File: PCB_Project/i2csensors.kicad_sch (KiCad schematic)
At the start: 19 parts, among them J2 ZE27-O3, J3 Motor_Connector, J4 Motor_Connector, J5 Motor_Connector, J6 Motor_Connector

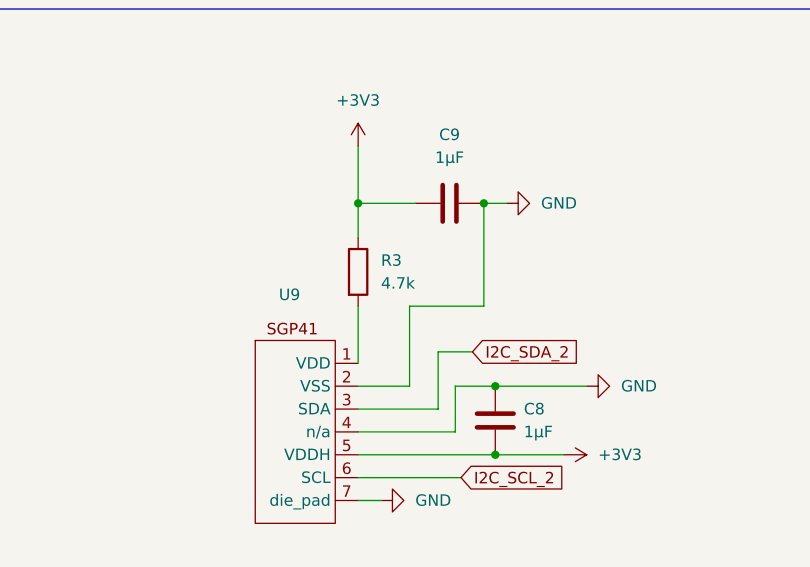
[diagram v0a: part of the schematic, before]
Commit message: Fixed resistor value for SGP41
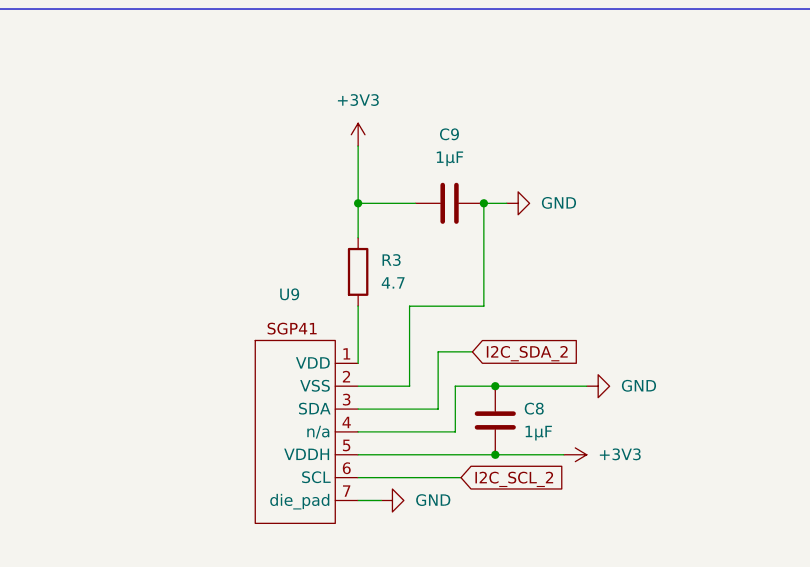
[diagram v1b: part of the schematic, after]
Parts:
- R3: value 4.7k -> 4.7
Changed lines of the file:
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@@
 			)
 		)
-		(property "Value" "4.7k"
+		(property "Value" "4.7"
 			(at 204.47 63.5 0)
 			(effects

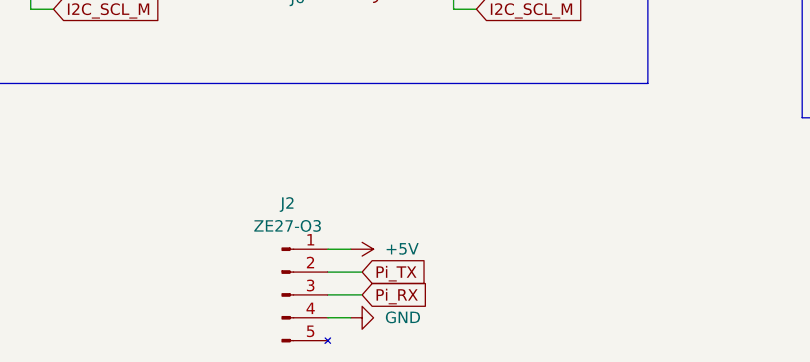
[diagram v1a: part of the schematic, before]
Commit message: Swapped Pi_RX and Pi_TX
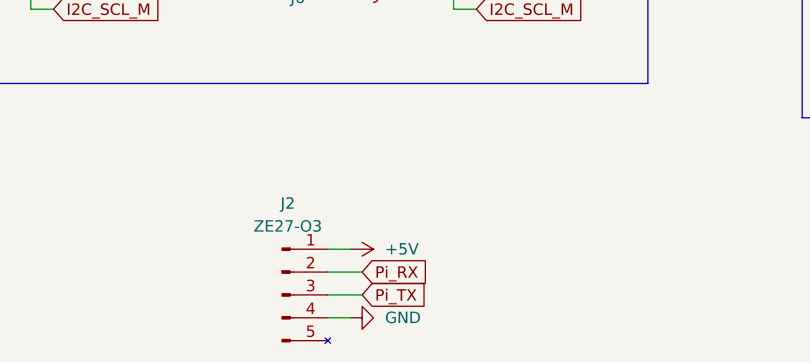
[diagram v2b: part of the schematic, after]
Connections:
- net Pi_RX: now also J2.2 (UART_TXD_(Out)); no longer J2.3 (UART_RX_(In))
- net Pi_TX: now also J2.3 (UART_RX_(In)); no longer J2.2 (UART_TXD_(Out))
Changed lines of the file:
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@@
 	(global_label "Pi_TX"
 		(shape input)
-		(at 93.98 162.56 0)
+		(at 93.98 165.1 0)
 		(fields_autoplaced yes)
 		(effects
@@
 		)
 		(property "Intersheetrefs" "${INTERSHEET_REFS}"
-			(at 101.9847 162.56 0)
+			(at 101.9847 165.1 0)
 			(effects
 				(font
@@
 	(global_label "Pi_RX"
 		(shape input)
-		(at 93.98 165.1 0)
+		(at 93.98 162.56 0)
 		(fields_autoplaced yes)
 		(effects
@@
 		)
 		(property "Intersheetrefs" "${INTERSHEET_REFS}"
-			(at 102.2871 165.1 0)
+			(at 102.2871 162.56 0)
 			(effects
 				(font

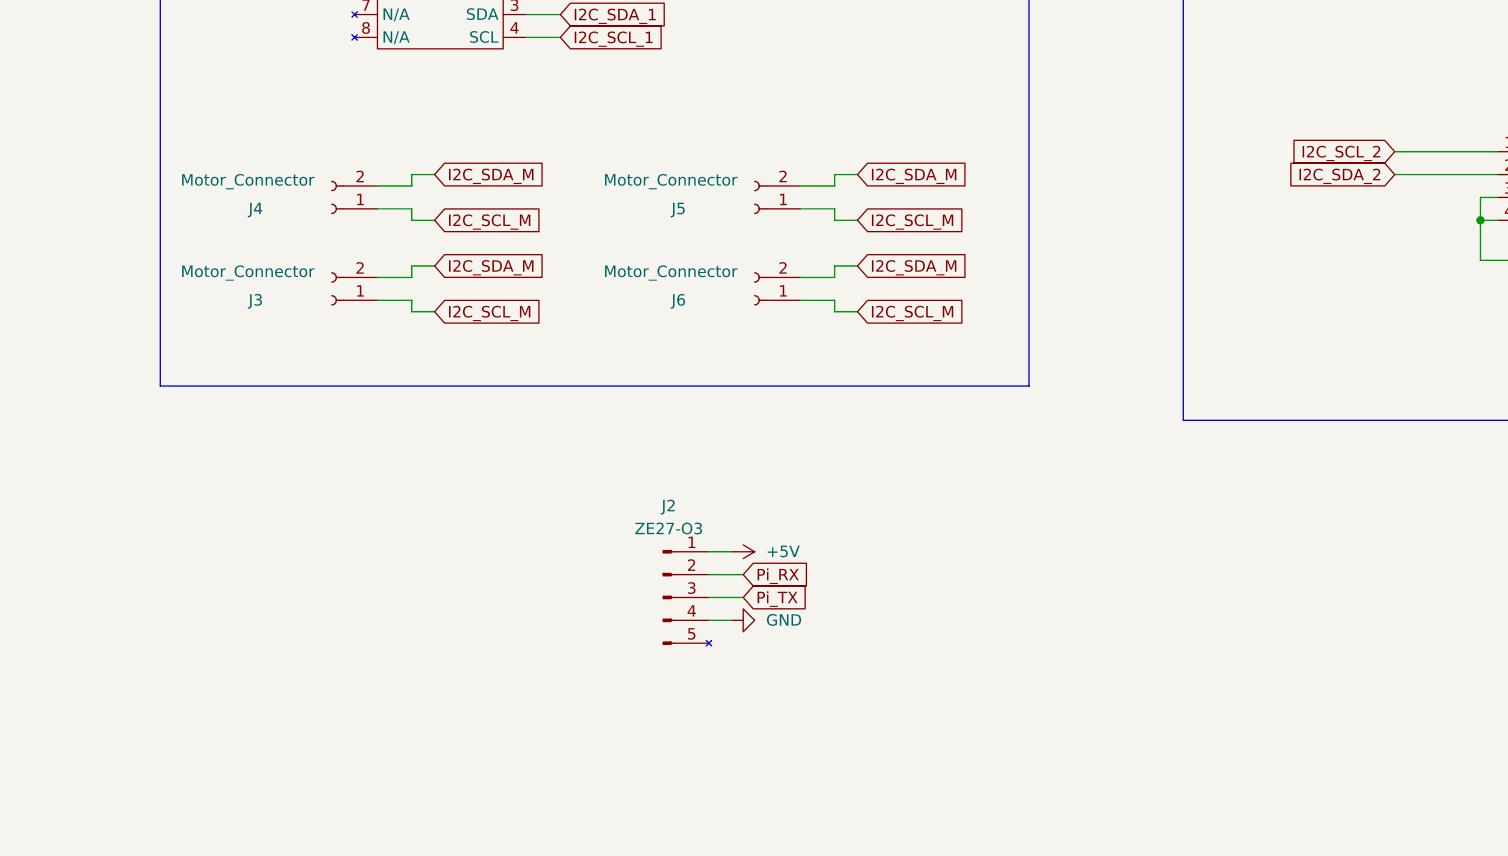
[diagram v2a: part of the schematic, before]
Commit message: added level shifters
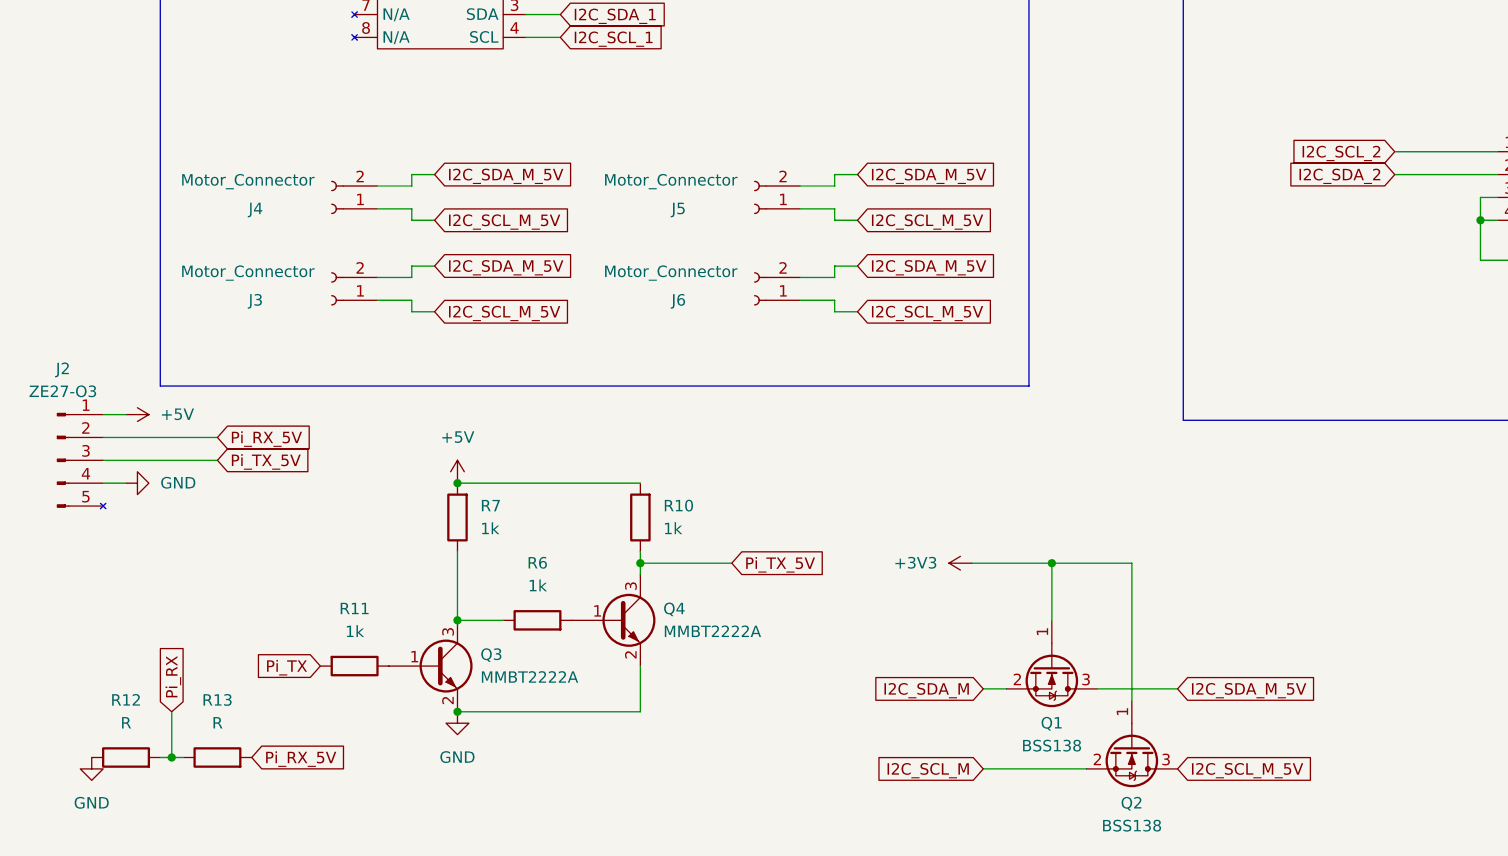
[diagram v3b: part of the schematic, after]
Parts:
- added Q1, Q2: BSS138, Package_TO_SOT_SMD:SOT-23, symbol Transistor_FET:BSS138
- added Q3, Q4: MMBT2222A, Package_TO_SOT_SMD:SOT-23, symbol Transistor_BJT:MMBT2222A
- added R10, R11, R6, R7: 1k, symbol Device:R
- added R12, R13: R, symbol Device:R
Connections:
- net +3V3: now also Q1.1 (G), Q2.1 (G)
- net +5V: now also R10.2, R7.2
- net GND: now also Q3.2 (E), Q4.2 (E), R12.1
- net I2C_SCL_M: now also Q2.2 (S); no longer J3.1 (Pin_1), J4.1 (Pin_1), J5.1 (Pin_1), J6.1 (Pin_1)
- net I2C_SDA_M: now also Q1.2 (S); no longer J3.2 (Pin_2), J4.2 (Pin_2), J5.2 (Pin_2), J6.2 (Pin_2)
- net Pi_RX: now also R12.2, R13.1; no longer J2.2 (UART_TXD_(Out))
- net Pi_TX: now also R11.2; no longer J2.3 (UART_RX_(In))
- new net: Q3.1 (B), R11.1
- new net: Q3.3 (C), R6.1, R7.1
- new net: Q4.1 (B), R6.2
- new net I2C_SCL_M_5V: J3.1 (Pin_1), J4.1 (Pin_1), J5.1 (Pin_1), J6.1 (Pin_1), Q2.3 (D)
- new net I2C_SDA_M_5V: J3.2 (Pin_2), J4.2 (Pin_2), J5.2 (Pin_2), J6.2 (Pin_2), Q1.3 (D)
- new net Pi_RX_5V: J2.2 (UART_TXD_(Out)), R13.2
- new net Pi_TX_5V: J2.3 (UART_RX_(In)), Q4.3 (C), R10.1
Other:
- moved on the sheet: J2

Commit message: footprints
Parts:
- R10, R11, R6, R7: footprint (none) -> Resistor_SMD:R_0402_1005Metric
- R12: value R -> 2k; footprint (none) -> Resistor_SMD:R_0402_1005Metric
- R13: value R -> 1k; footprint (none) -> Resistor_SMD:R_0402_1005Metric
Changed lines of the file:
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@@
 			)
 		)
-		(property "Value" "R"
+		(property "Value" "2k"
 			(at 25.4 179.07 90)
 			(effects
@@
 			)
 		)
-		(property "Footprint" ""
+		(property "Footprint" "Resistor_SMD:R_0402_1005Metric"
 			(at 25.4 184.658 90)
 			(effects
@@
 			)
 		)
-		(property "Footprint" ""
+		(property "Footprint" "Resistor_SMD:R_0402_1005Metric"
 			(at 50.8 170.942 90)
 			(effects
@@
 			)
 		)
-		(property "Footprint" ""
+		(property "Footprint" "Resistor_SMD:R_0402_1005Metric"
 			(at 84.328 156.21 90)
 			(effects
@@
 			)
 		)
-		(property "Footprint" ""
+		(property "Footprint" "Resistor_SMD:R_0402_1005Metric"
 			(at 64.008 156.21 90)
 			(effects
@@
 			)
 		)
-		(property "Footprint" ""
+		(property "Footprint" "Resistor_SMD:R_0402_1005Metric"
 			(at 71.12 169.418 90)
 			(effects
@@
 			)
 		)
-		(property "Value" "R"
+		(property "Value" "1k"
 			(at 35.56 179.07 90)
 			(effects
@@
 			)
 		)
-		(property "Footprint" ""
+		(property "Footprint" "Resistor_SMD:R_0402_1005Metric"
 			(at 35.56 184.658 90)
 			(effects

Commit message: soldering it to the board
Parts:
- J2: footprint Connector_JST:JST_EH_B5B-EH-A_1x05_P2.50mm_Vertical -> Connector_PinHeader_2.00mm:PinHeader_1x05_P2.00mm_Vertical
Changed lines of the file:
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@@
 			)
 		)
-		(property "Footprint" "Connector_JST:JST_EH_B5B-EH-A_1x05_P2.50mm_Vertical"
+		(property "Footprint" "Connector_PinHeader_2.00mm:PinHeader_1x05_P2.00mm_Vertical"
 			(at 17.78 149.86 0)
 			(effects

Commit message: working on final board
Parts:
- removed J2: ZE27-O3, Connector_PinHeader_2.00mm:PinHeader_1x05_P2.00mm_Vertical, symbol Connector:Conn_01x05_Pin
- removed Q1, Q2: BSS138, Package_TO_SOT_SMD:SOT-23, symbol Transistor_FET:BSS138
- removed Q3, Q4: MMBT2222A, Package_TO_SOT_SMD:SOT-23, symbol Transistor_BJT:MMBT2222A
- removed R10, R11, R13, R6, R7: 1k, Resistor_SMD:R_0402_1005Metric, symbol Device:R
- removed R12: 2k, Resistor_SMD:R_0402_1005Metric, symbol Device:R
- C2: renamed from C11; value 1 µF -> 1µF
- U6: renamed from U11; footprint Sensor:SOIC127P600X175-8N_ADT7410TRZ-REEL -> Sensor:SOIC127P600X175-8N
- renumbered C12 to C1, C9 to C3, C10 to C4, C8 to C5, C15 to C6, C13 to C7, C14 to C8, J4 to J1, J5 to J2, J6 to J4, R3 to R7, U12 to U2, U9 to U3, U8 to U4, U10 to U5
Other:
- moved on the sheet: C3

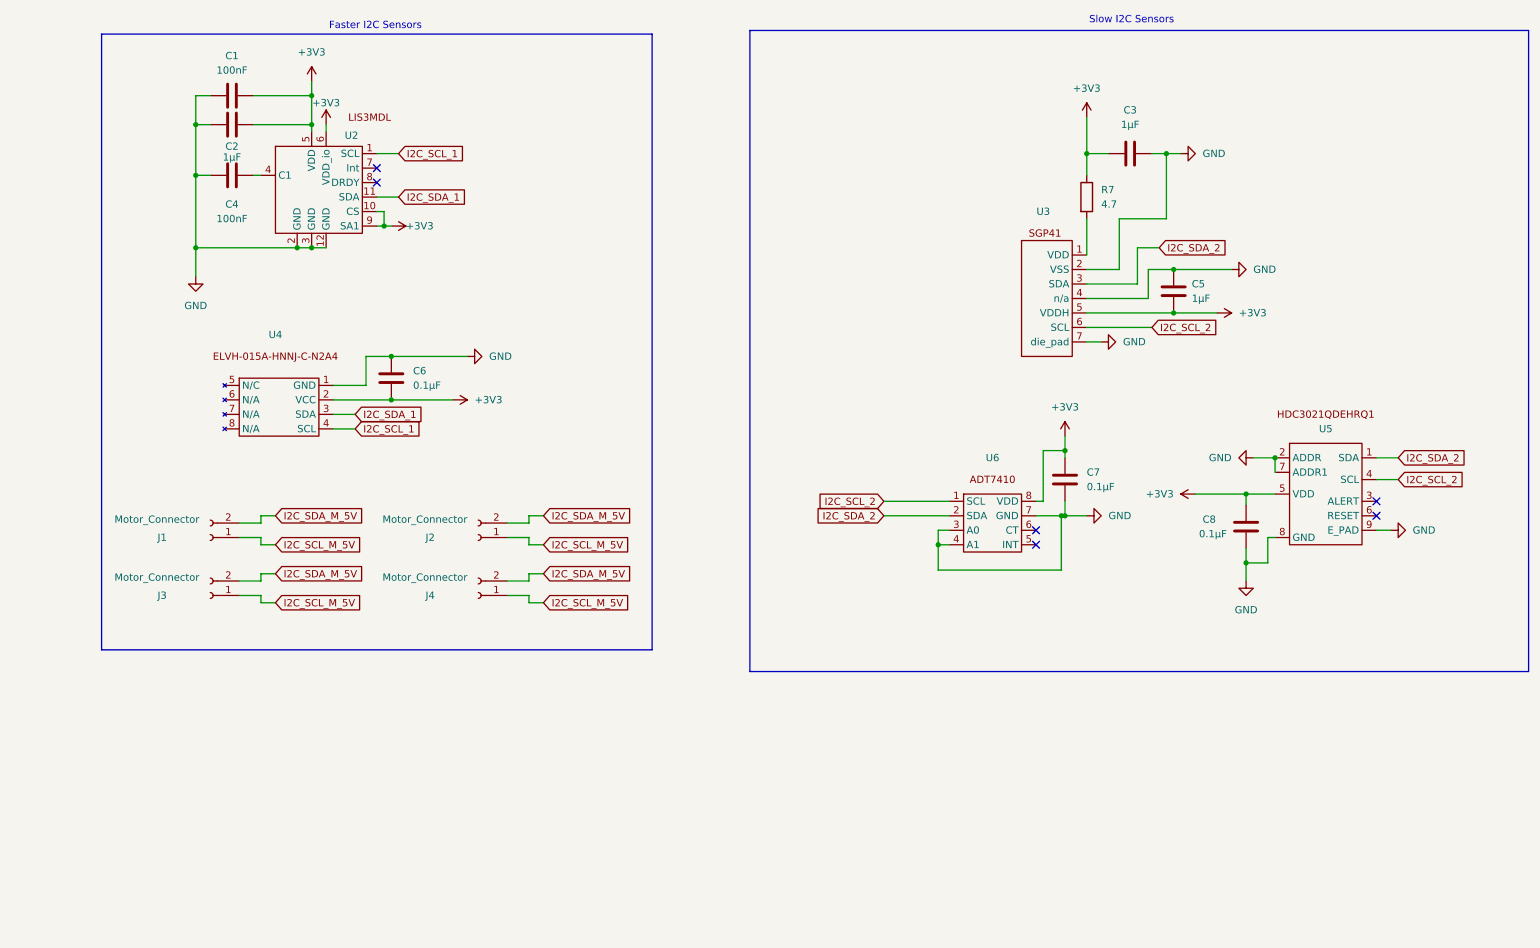
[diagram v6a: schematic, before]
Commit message: power distribution done
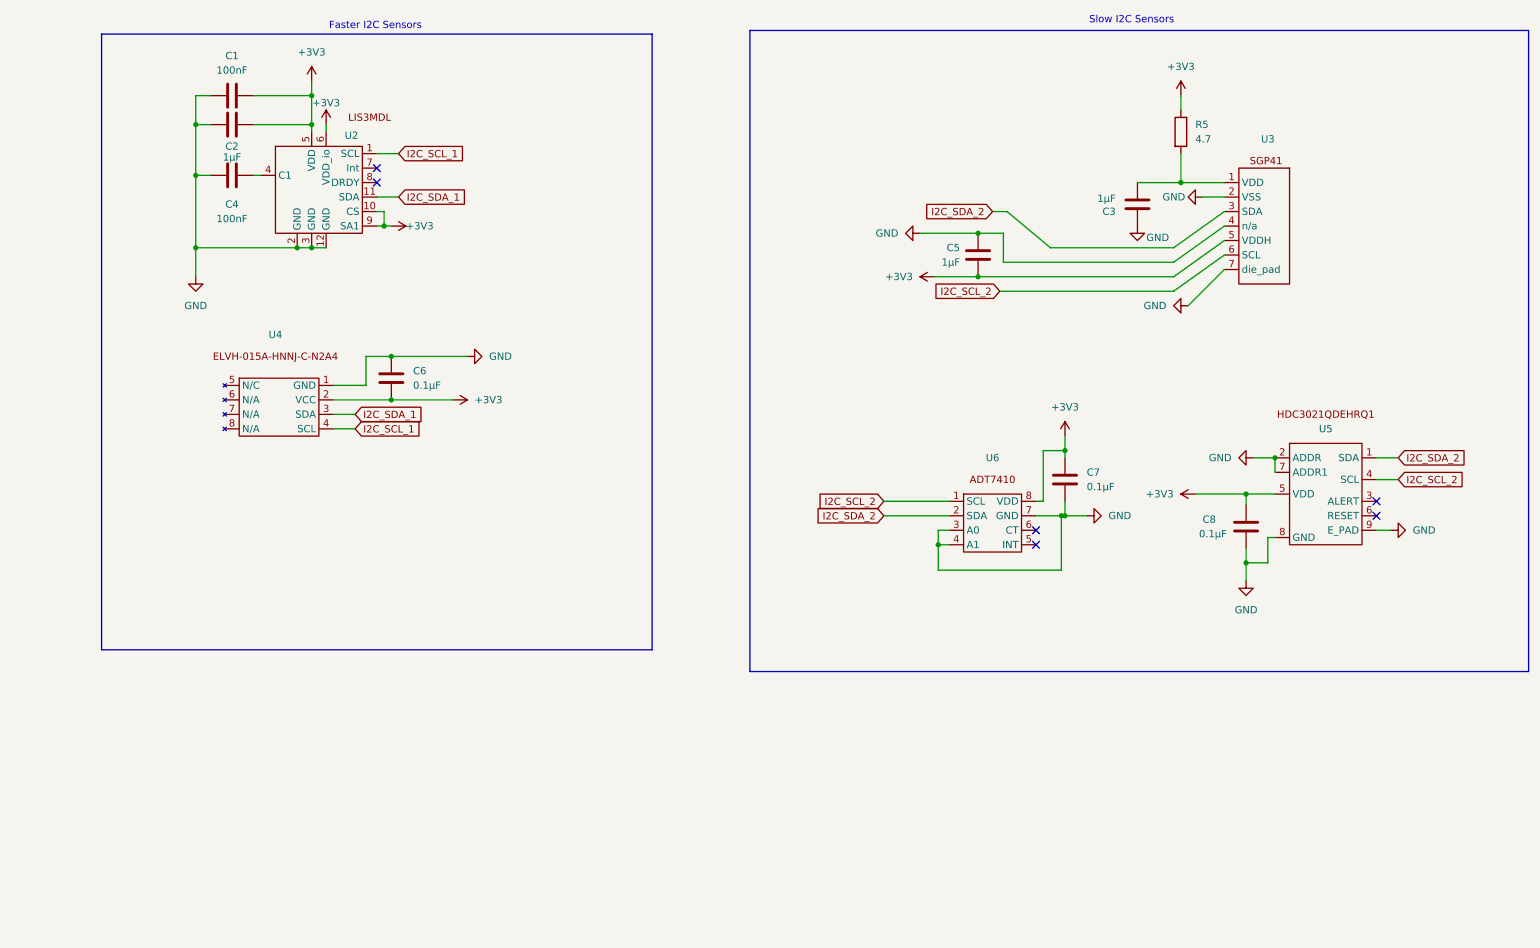
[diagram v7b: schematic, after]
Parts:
- removed J1, J2, J3, J4: Motor_Connector, Connector_JST:JST_PH_B2B-PH-K_1x02_P2.00mm_Vertical, symbol Connector:Conn_01x02_Socket
- removed R7: 4.7, Resistor_SMD:R_0402_1005Metric, symbol Device:R
- added R5: 4.7, Resistor_SMD:R_0603_1608Metric, symbol Device:R
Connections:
- net +3V3: now also R5.1; no longer C3.1
- net at U3.1 (VDD): now also C3.1, R5.2
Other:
- moved on the sheet: C5, U3

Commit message: power baby
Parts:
- removed C6: 0.1µF, Capacitor_SMD:C_0402_1005Metric, symbol Device:C
- renumbered C4 to C3, C3 to C4, C7 to C6, C8 to C7, U3 to U2, U2 to U3
